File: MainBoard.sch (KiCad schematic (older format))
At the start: 79 parts, among them J1 DB25, P1 BOOT, P10 CONN_01X03, P11 CONN_01X03, P12 CONN_01X03, P13 CONN_01X03, P14 CONN_01X02, P15 CONN_02X07, P16 CONN_02X05, P17 CONN_01X04, P18 CONN_01X03, P2 CONN_01X04, P3 CONN_01X05, P4 HOLE, P5 HOLE, P6 HOLE, P7 HOLE, P8 CONN_01X02, P9 CONN_01X03, Q1 BSS138, Q2 BSS138, Q3 DMN65D8L, SW1 RESET, U1 mp2307, U10 SI4425DDY, U2 DYS_mini_ESC, U3 DYS_mini_ESC, U4 DYS_mini_ESC, U5 DYS_mini_ESC, U6 TLV1117LV33, U7 TENDA_P200, U8 pca9685, U9 STM32F103CBT6, Y1 8MHz

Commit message: Add BOM
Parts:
- C1: DigiKey (none) -> 445-8867-1-ND; Part # 445-8867-1-ND -> (none); Vender DigiKey -> (none)
- C12: value C -> 10uF
- C5: DigiKey (none) -> 1276-6786-1-ND; Part # 1276-6786-1-ND -> (none); Vender DigiKey -> (none)
- C6, C7, C8, C9: value CP1 -> 100uF
- D1, D2: DigiKey (none) -> 160-1426-1-ND
- J1: DigiKey (none) -> A35111-ND
- L1: DigiKey (none) -> ASPI-0630LR-100M-T15CT-ND; Part # ASPI-0630LR-100M-T15CT-ND -> (none); Vender DigiKey -> (none)
- P17, P2: DigiKey (none) -> 455-2249-ND
- P3: DigiKey (none) -> 455-2270-ND
- Q1, Q2: DigiKey (none) -> BSS138CT-ND; Mouser (none) -> 512-BSS138
- Q3: DigiKey (none) -> DMN65D8L-7DICT-ND
- R3: DigiKey (none) -> YAG2318CT-ND
- R4: DigiKey (none) -> 311-2584-1-ND
- RN1, RN2, RN3: DigiKey (none) -> 742C083103JPCT-ND
- SW1: Part # 2220 -> (none); Vender deviceMart -> (none); deviceMart (none) -> 2220
- U1: Mouser (none) -> 946-MP2307DNLF; Part # 946-MP2307DNLF -> (none); Vender Mouser -> (none)
- U10: DigiKey (none) -> SI4425DDY-T1-GE3CT-ND
- U6: DigiKey (none) -> 296-28778-1-ND; Mouser (none) -> 595-TLV1117LV33DCYR
- U8: DigiKey (none) -> 568-5931-1-ND
- U9: DigiKey (none) -> 497-6288-ND
- Y1: DigiKey (none) -> 535-9720-1-ND; Part # 535-9720-1-ND -> (none); Vender DigiKey -> (none)
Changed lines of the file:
@@
 P 4475 1000
 F 0 "C6" H 4500 1100 50  0000 L CNN
-F 1 "CP1" H 4500 900 50  0000 L CNN
+F 1 "100uF" H 4500 900 50  0000 L CNN
 F 2 "Capacitors_SMD:c_elec_6.3x4.5" H 4475 1000 50  0001 C CNN
 F 3 "" H 4475 1000 50  0000 C CNN
@@
 P 4475 1775
 F 0 "C7" H 4500 1875 50  0000 L CNN
-F 1 "CP1" H 4500 1675 50  0000 L CNN
+F 1 "100uF" H 4500 1675 50  0000 L CNN
 F 2 "Capacitors_SMD:c_elec_6.3x4.5" H 4475 1775 50  0001 C CNN
 F 3 "" H 4475 1775 50  0000 C CNN
@@
 P 4475 2550
 F 0 "C8" H 4500 2650 50  0000 L CNN
-F 1 "CP1" H 4500 2450 50  0000 L CNN
+F 1 "100uF" H 4500 2450 50  0000 L CNN
 F 2 "Capacitors_SMD:c_elec_6.3x4.5" H 4475 2550 50  0001 C CNN
 F 3 "" H 4475 2550 50  0000 C CNN
@@
 P 4475 3350
 F 0 "C9" H 4500 3450 50  0000 L CNN
-F 1 "CP1" H 4500 3250 50  0000 L CNN
+F 1 "100uF" H 4500 3250 50  0000 L CNN
 F 2 "Capacitors_SMD:c_elec_6.3x4.5" H 4475 3350 50  0001 C CNN
 F 3 "" H 4475 3350 50  0000 C CNN
@@
 F 2 "Housings_SOIC:SOIC-8-1EP_3.9x4.9mm_Pitch1.27mm" H 1825 1325 60  0001 C CNN
 F 3 "https://cdn-shop.adafruit.com/datasheets/MP2307_r1.9.pdf" H 1825 1325 60  0001 C CNN
-F 4 "Mouser" H 1800 1400 60  0001 C CNN "Vender"
-F 5 "946-MP2307DNLF" H 1800 1400 60  0001 C CNN "Part #"
+F 4 "946-MP2307DNLF" H 1800 1400 60  0001 C CNN "Mouser"
 	1    1800 1400
 	1    0    0    -1
@@
 F 2 "Capacitors_SMD:C_1206" H 1025 1275 50  0001 C CNN
 F 3 "" H 1025 1275 50  0000 C CNN
-F 4 "DigiKey" H 1025 1275 60  0001 C CNN "Vender"
-F 5 "445-8867-1-ND" H 1025 1275 60  0001 C CNN "Part #"
+F 4 "445-8867-1-ND" H 1025 1275 60  0001 C CNN "DigiKey"
 	1    1025 1275
 	1    0    0    -1
@@
 F 2 "footprint:ASPI-0630LR" H 2900 1300 50  0001 C CNN
 F 3 "http://abracon.com/Support/PackageDrawing/Magnetics/ASPI-0630LR.PDF" H 2900 1300 50  0001 C CNN
-F 4 "DigiKey" V 2900 1300 60  0001 C CNN "Vender"
-F 5 "ASPI-0630LR-100M-T15CT-ND" V 2900 1300 60  0001 C CNN "Part #"
+F 4 "ASPI-0630LR-100M-T15CT-ND" V 2900 1300 60  0001 C CNN "DigiKey"
 	1    2900 1300
 	0    -1   -1   0
@@
 F 2 "Capacitors_SMD:C_0603" V 2605 2075 50  0001 C CNN
 F 3 "" H 2675 2075 50  0000 C CNN
+F 4 "YAG2318CT-ND" H 2675 2075 60  0001 C CNN "DigiKey"
 	1    2675 2075
 	1    0    0    -1
@@
 F 2 "Capacitors_SMD:C_0805" H 3240 1984 50  0001 L CNN
 F 3 "" H 3125 2075 50  0000 C CNN
-F 4 "DigiKey" H 3125 2075 60  0001 C CNN "Vender"
-F 5 "1276-6786-1-ND" H 3125 2075 60  0001 C CNN "Part #"
+F 4 "1276-6786-1-ND" H 3125 2075 60  0001 C CNN "DigiKey"
 	1    3125 2075
 	1    0    0    -1
@@
 F 2 "Capacitors_SMD:C_0603" V 2830 1500 50  0001 C CNN
 F 3 "" H 2900 1500 50  0000 C CNN
+F 4 "311-2584-1-ND" V 2900 1500 60  0001 C CNN "DigiKey"
 	1    2900 1500
 	0    1    1    0
@@
 F 2 "Connect:DB25FC" H 15254 2814 50  0001 L CNN
 F 3 "" H 15075 2900 50  0000 C CNN
+F 4 "A35111-ND" H 15075 2900 60  0001 C CNN "DigiKey"
 	1    15075 2900
 	1    0    0    -1
@@
 F 2 "TO_SOT_Packages_SMD:SOT-223" H 2100 3475 50  0001 C CIN
 F 3 "" H 2100 3375 50  0000 C CNN
+F 4 "595-TLV1117LV33DCYR" H 2100 3375 60  0001 C CNN "Mouser"
+F 5 "296-28778-1-ND" H 2100 3375 60  0001 C CNN "DigiKey"
 	1    2100 3375
 	1    0    0    -1
@@
 F 2 "LEDs:LED_0805" H 966 5375 50  0001 C CNN
 F 3 "" H 975 5250 50  0000 C CNN
+F 4 "160-1426-1-ND" H 975 5250 60  0001 C CNN "DigiKey"
 	1    975  5250
 	1    0    0    -1
@@
 F 2 "LEDs:LED_0805" H 966 5575 50  0001 C CNN
 F 3 "" H 975 5450 50  0000 C CNN
+F 4 "160-1426-1-ND" H 975 5450 60  0001 C CNN "DigiKey"
 	1    975  5450
 	-1   0    0    1
@@
 F 2 "Housings_SSOP:TSSOP-28_4.4x9.7mm_Pitch0.65mm" H 9225 625 60  0001 C CNN
 F 3 "https://cdn-shop.adafruit.com/datasheets/PCA9685.pdf" H 9225 625 60  0001 C CNN
+F 4 "568-5931-1-ND" H 8525 1675 60  0001 C CNN "DigiKey"
 	1    8525 1675
 	1    0    0    -1
@@
 P 7450 1075
 F 0 "C12" H 7200 1150 50  0000 L CNN
-F 1 "C" H 7250 1000 50  0000 L CNN
+F 1 "10uF" H 7250 1000 50  0000 L CNN
 F 2 "Capacitors_SMD:C_0603" H 7565 984 50  0001 L CNN
 F 3 "" H 7450 1075 50  0000 C CNN
@@
 F 2 "Resistors_SMD:R_Array_Concave_4x0603" V 9800 1125 50  0001 C CNN
 F 3 "" H 9525 1125 50  0000 C CNN
+F 4 "742C083103JPCT-ND" V 9525 1125 60  0001 C CNN "DigiKey"
 	1    9525 1125
 	0    -1   1    0
@@
 F 2 "Resistors_SMD:R_Array_Concave_4x0603" V 9800 1575 50  0001 C CNN
 F 3 "" H 9525 1575 50  0000 C CNN
+F 4 "742C083103JPCT-ND" V 9525 1575 60  0001 C CNN "DigiKey"
 	1    9525 1575
 	0    -1   1    0
@@
 F 2 "Resistors_SMD:R_Array_Concave_4x0603" V 9800 2025 50  0001 C CNN
 F 3 "" H 9525 2025 50  0000 C CNN
+F 4 "742C083103JPCT-ND" V 9525 2025 60  0001 C CNN "DigiKey"
 	1    9525 2025
 	0    1    1    0
@@
 F 2 "TO_SOT_Packages_SMD:SOT-23" H 1650 6625 50  0001 L CIN
 F 3 "" H 1450 6700 50  0000 L CNN
+F 4 "512-BSS138" V 1450 6700 60  0001 C CNN "Mouser"
+F 5 "BSS138CT-ND" V 1450 6700 60  0001 C CNN "DigiKey"
 	1    1450 6700
 	0    1    1    0
@@
 F 2 "TO_SOT_Packages_SMD:SOT-23" H 3425 6625 50  0001 L CIN
 F 3 "" H 3225 6700 50  0000 L CNN
+F 4 "512-BSS138" V 3225 6700 60  0001 C CNN "Mouser"
+F 5 "BSS138CT-ND" V 3225 6700 60  0001 C CNN "DigiKey"
 	1    3225 6700
 	0    1    1    0
@@
 F 2 "Housings_QFP:LQFP-48_7x7mm_Pitch0.5mm" H 10325 9100 50  0000 C CNN
 F 3 "" H 12250 7475 50  0000 C CNN
+F 4 "497-6288-ND" H 12250 7475 60  0001 C CNN "DigiKey"
 	1    12250 7475
 	1    0    0    -1
@@
 F 2 "footprint:crystal_maple" H 7950 6725 50  0001 C CNN
 F 3 "" H 7950 6725 50  0000 C CNN
-F 4 "DigiKey" V 7950 6725 60  0001 C CNN "Vender"
-F 5 "535-9720-1-ND" V 7950 6725 60  0001 C CNN "Part #"
+F 4 "535-9720-1-ND" V 7950 6725 60  0001 C CNN "DigiKey"
 	1    7950 6725
 	0    1    1    0
@@
 F 2 "footprint:smd_push" H 8700 6275 50  0001 C CNN
 F 3 "" H 8700 6275 50  0000 C CNN
-F 4 "deviceMart" H 8700 6075 60  0001 C CNN "Vender"
-F 5 "2220" H 8700 6075 60  0001 C CNN "Part #"
+F 4 "2220" H 8700 6075 60  0001 C CNN "deviceMart"
 	1    8700 6075
 	1    0    0    -1
@@
 F 2 "Connectors_JST:JST_XH_B04B-XH-A_04x2.50mm_Straight" H 1578 7579 50  0001 L CNN
 F 3 "" H 1500 7675 50  0000 C CNN
+F 4 "455-2249-ND" H 1500 7675 60  0001 C CNN "DigiKey"
 	1    1500 7675
 	1    0    0    1
@@
 F 2 "Connectors_JST:JST_XH_B05B-XH-A_05x2.50mm_Straight" H 1578 8204 50  0001 L CNN
 F 3 "" H 1500 8300 50  0000 C CNN
+F 4 "455-2270-ND" H 1500 8300 60  0001 C CNN "DigiKey"
 	1    1500 8300
 	1    0    0    -1
@@
 F 2 "SMD_Packages:SOIC-8-N" H 5425 4250 60  0001 C CNN
 F 3 "" H 5425 4250 60  0001 C CNN
+F 4 "SI4425DDY-T1-GE3CT-ND" H 5425 4250 60  0001 C CNN "DigiKey"
 	1    5425 4250
 	1    0    0    -1
@@
 F 2 "TO_SOT_Packages_SMD:SOT-23" H 4781 4809 50  0001 L CNN
 F 3 "" H 4575 4900 50  0000 C CNN
+F 4 "DMN65D8L-7DICT-ND" H 4575 4900 60  0001 C CNN "DigiKey"
 	1    4575 4900
 	1    0    0    -1
@@
 F 2 "Connectors_JST:JST_XH_B04B-XH-A_04x2.50mm_Straight" H 1578 8829 50  0001 L CNN
 F 3 "" H 1500 8925 50  0000 C CNN
+F 4 "455-2249-ND" H 1500 8925 60  0001 C CNN "DigiKey"
 	1    1500 8925
 	1    0    0    -1

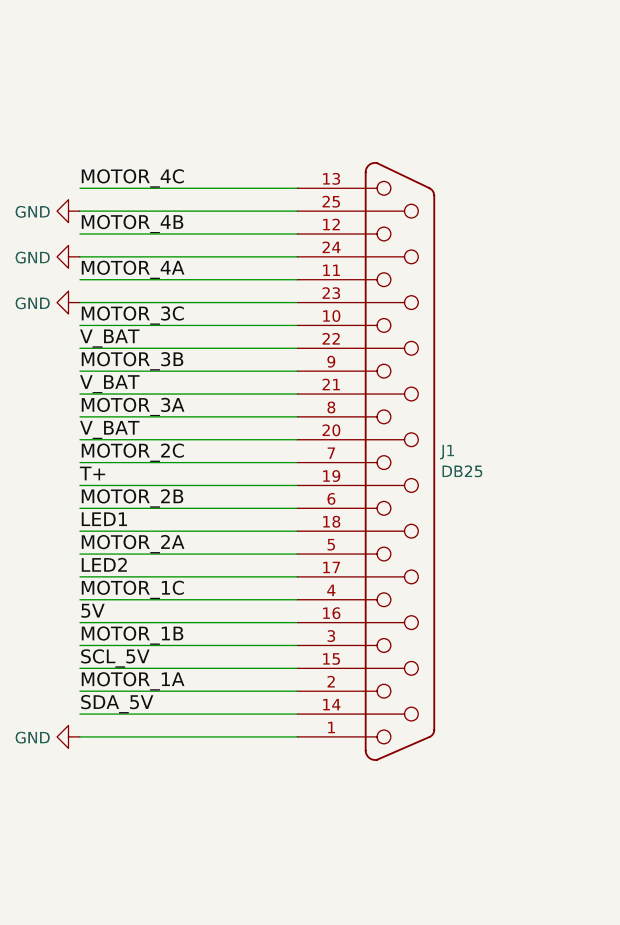
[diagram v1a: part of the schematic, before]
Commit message: Change db25 footprint
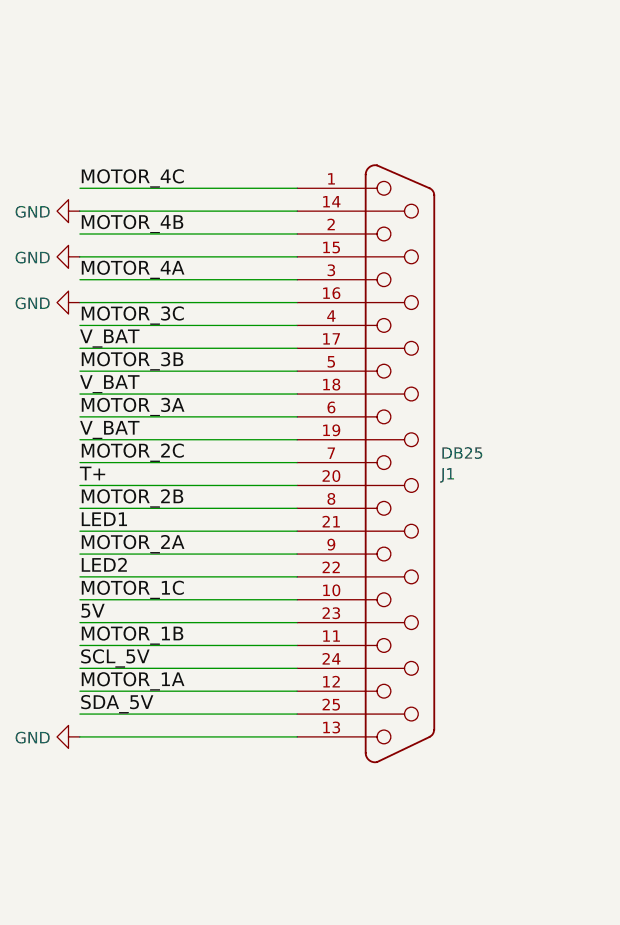
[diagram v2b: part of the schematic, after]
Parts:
- J1: footprint Connect:DB25FC -> footprint:DB_25M
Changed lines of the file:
@@
 F 0 "J1" H 15254 2951 50  0000 L CNN
 F 1 "DB25" H 15254 2860 50  0000 L CNN
-F 2 "Connect:DB25FC" H 15254 2814 50  0001 L CNN
+F 2 "footprint:DB_25M" H 15254 2814 50  0001 L CNN
 F 3 "" H 15075 2900 50  0000 C CNN
 F 4 "A35111-ND" H 15075 2900 60  0001 C CNN "DigiKey"
 	1    15075 2900
-	1    0    0    -1
+	1    0    0    1
 $EndComp
 $Comp

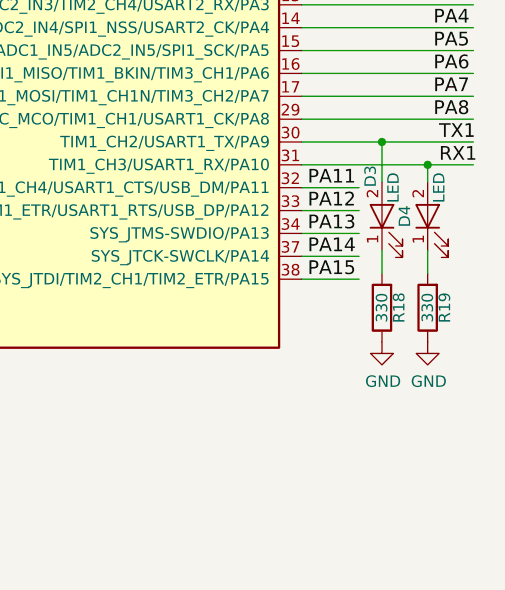
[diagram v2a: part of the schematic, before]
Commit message: pull up rx/tx indicate led & change esc capacitor size
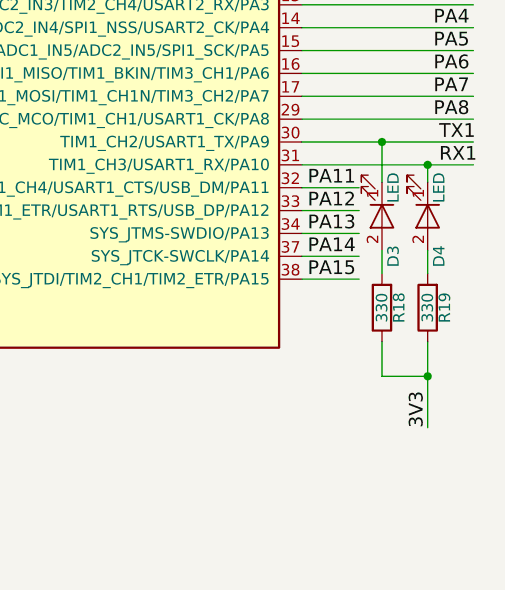
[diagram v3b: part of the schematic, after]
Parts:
- C6, C7, C8, C9: footprint Capacitors_SMD:c_elec_6.3x4.5 -> Capacitors_SMD:CP_Elec_8x10
- D3, D4: DigiKey (none) -> 160-1426-1-ND
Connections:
- wire segments 295 -> 298
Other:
- moved on the sheet: D3, D4
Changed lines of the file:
@@
 F 0 "C6" H 4500 1100 50  0000 L CNN
 F 1 "100uF" H 4500 900 50  0000 L CNN
-F 2 "Capacitors_SMD:c_elec_6.3x4.5" H 4475 1000 50  0001 C CNN
+F 2 "Capacitors_SMD:CP_Elec_8x10" H 4475 1000 50  0001 C CNN
 F 3 "" H 4475 1000 50  0000 C CNN
 	1    4475 1000
@@
 F 0 "C7" H 4500 1875 50  0000 L CNN
 F 1 "100uF" H 4500 1675 50  0000 L CNN
-F 2 "Capacitors_SMD:c_elec_6.3x4.5" H 4475 1775 50  0001 C CNN
+F 2 "Capacitors_SMD:CP_Elec_8x10" H 4475 1775 50  0001 C CNN
 F 3 "" H 4475 1775 50  0000 C CNN
 	1    4475 1775
@@
 F 0 "C8" H 4500 2650 50  0000 L CNN
 F 1 "100uF" H 4500 2450 50  0000 L CNN
-F 2 "Capacitors_SMD:c_elec_6.3x4.5" H 4475 2550 50  0001 C CNN
+F 2 "Capacitors_SMD:CP_Elec_8x10" H 4475 2550 50  0001 C CNN
 F 3 "" H 4475 2550 50  0000 C CNN
 	1    4475 2550
@@
 F 0 "C9" H 4500 3450 50  0000 L CNN
 F 1 "100uF" H 4500 3250 50  0000 L CNN
-F 2 "Capacitors_SMD:c_elec_6.3x4.5" H 4475 3350 50  0001 C CNN
+F 2 "Capacitors_SMD:CP_Elec_8x10" H 4475 3350 50  0001 C CNN
 F 3 "" H 4475 3350 50  0000 C CNN
 	1    4475 3350
@@
 P 15500 8600
 F 0 "D3" H 15675 8650 50  0000 C CNN
-F 1 "LED" H 15625 8550 50  0000 C CNN
+F 1 "LED" H 15375 8650 50  0000 C CNN
 F 2 "LEDs:LED_0805" H 15491 8725 50  0001 C CNN
 F 3 "" H 15500 8600 50  0000 C CNN
+F 4 "160-1426-1-ND" H 15500 8600 60  0001 C CNN "DigiKey"
 	1    15500 8600
-	0    -1   -1   0
+	0    1    1    0
 $EndComp
 $Comp
@@
 $EndComp
 $Comp
-L GND #PWR020
-U 1 1 58782956
-P 15500 9150
-F 0 "#PWR020" H 15500 8900 50  0001 C CNN
-F 1 "GND" H 15505 8977 50  0000 C CNN
-F 2 "" H 15500 9150 50  0000 C CNN
-F 3 "" H 15500 9150 50  0000 C CNN
-	1    15500 9150
-	1    0    0    -1
-$EndComp
-$Comp
 L LED D4
 U 1 1 58783046
 P 15700 8600
-F 0 "D4" H 15700 8700 50  0000 C CNN
-F 1 "LED" H 15825 8550 50  0000 C CNN
+F 0 "D4" H 15875 8650 50  0000 C CNN
+F 1 "LED" H 15575 8650 50  0000 C CNN
 F 2 "LEDs:LED_0805" H 15691 8725 50  0001 C CNN
 F 3 "" H 15700 8600 50  0000 C CNN
+F 4 "160-1426-1-ND" H 15700 8600 60  0001 C CNN "DigiKey"
 	1    15700 8600
-	0    -1   -1   0
+	0    1    1    0
 $EndComp
 $Comp
@@
 	1    15700 9000
 	-1   0    0    1
-$EndComp
-$Comp
-L GND #PWR021
-U 1 1 5878356B
-P 15700 9150
-F 0 "#PWR021" H 15700 8900 50  0001 C CNN
-F 1 "GND" H 15705 8977 50  0000 C CNN
-F 2 "" H 15700 9150 50  0000 C CNN
-F 3 "" H 15700 9150 50  0000 C CNN
-	1    15700 9150
-	1    0    0    -1
 $EndComp
 $Comp
@@
 NoConn ~ 9175 2575
 $Comp
-L GND #PWR022
+L GND #PWR020
 U 1 1 5873F101
 P 850 8775
-F 0 "#PWR022" H 850 8525 50  0001 C CNN
+F 0 "#PWR020" H 850 8525 50  0001 C CNN
 F 1 "GND" V 855 8647 50  0000 R CNN
 F 2 "" H 850 8775 50  0000 C CNN
@@
 PA2
 $Comp
-L GND #PWR023
+L GND #PWR021
 U 1 1 58763433
 P 2375 8625
-F 0 "#PWR023" H 2375 8375 50  0001 C CNN
+F 0 "#PWR021" H 2375 8375 50  0001 C CNN
 F 1 "GND" V 2380 8497 50  0000 R CNN
 F 2 "" H 2375 8625 50  0000 C CNN
@@
 PA8
 $Comp
-L GND #PWR024
+L GND #PWR022
 U 1 1 58798B24
 P 2375 8150
-F 0 "#PWR024" H 2375 7900 50  0001 C CNN
+F 0 "#PWR022" H 2375 7900 50  0001 C CNN
 F 1 "GND" V 2380 8022 50  0000 R CNN
 F 2 "" H 2375 8150 50  0000 C CNN
@@
 T+
 $Comp
-L GND #PWR025
+L GND #PWR023
 U 1 1 5879DBCB
 P 13675 2000
-F 0 "#PWR025" H 13675 1750 50  0001 C CNN
+F 0 "#PWR023" H 13675 1750 50  0001 C CNN
 F 1 "GND" V 13680 1872 50  0000 R CNN
 F 2 "" H 13675 2000 50  0000 C CNN
@@
 	14625 2800 13675 2800
 $Comp
-L GND #PWR026
+L GND #PWR024
 U 1 1 5879EE38
 P 13675 1800
-F 0 "#PWR026" H 13675 1550 50  0001 C CNN
+F 0 "#PWR024" H 13675 1550 50  0001 C CNN
 F 1 "GND" V 13680 1672 50  0000 R CNN
 F 2 "" H 13675 1800 50  0000 C CNN
@@
 	14625 3000 13675 3000
 $Comp
-L GND #PWR027
+L GND #PWR025
 U 1 1 5879F7DF
 P 13675 2200
-F 0 "#PWR027" H 13675 1950 50  0001 C CNN
+F 0 "#PWR025" H 13675 1950 50  0001 C CNN
 F 1 "GND" V 13680 2072 50  0000 R CNN
 F 2 "" H 13675 2200 50  0000 C CNN
@@
 	14625 4100 13675 4100
 $Comp
-L GND #PWR028
+L GND #PWR026
 U 1 1 587A1F4F
 P 13675 4100
-F 0 "#PWR028" H 13675 3850 50  0001 C CNN
+F 0 "#PWR026" H 13675 3850 50  0001 C CNN
 F 1 "GND" V 13680 3972 50  0000 R CNN
 F 2 "" H 13675 4100 50  0000 C CNN
@@
 NoConn ~ 8800 8775
 NoConn ~ 8800 8875
+Wire Wire Line
+	15700 9150 15700 9525
+Wire Wire Line
+	15500 9150 15500 9300
+Wire Wire Line
+	15500 9300 15700 9300
+Connection ~ 15700 9300
+Text Label 15700 9525 1    60   ~ 0
+3V3
 $EndSCHEMATC
